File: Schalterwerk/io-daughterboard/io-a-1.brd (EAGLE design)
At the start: 80 x 30.5 mm, 34 parts, among them Q1 BSS123, Q2 BSS123, Q3 BSS123, Q4 BSS123, Q5 BSS123, Q6 BSS123, Q7 BSS123, Q8 BSS123, U1 74HC166, U2 74HC166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

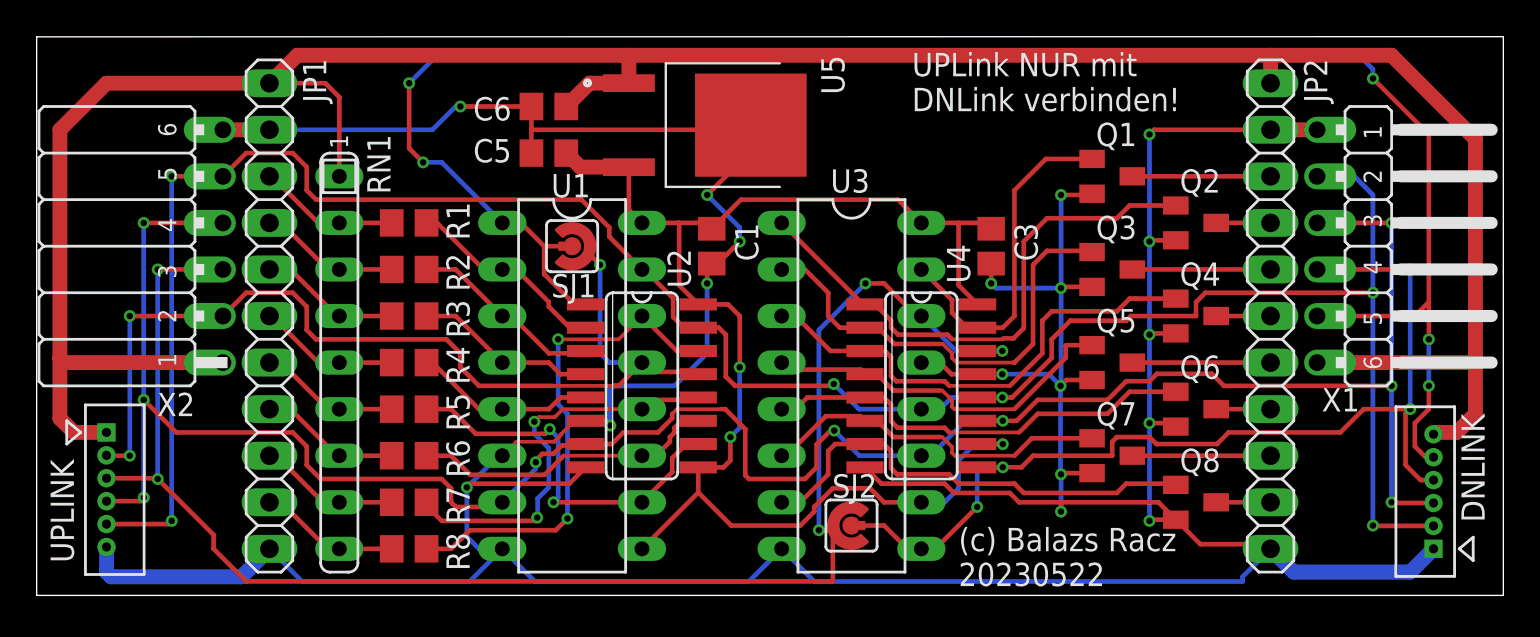
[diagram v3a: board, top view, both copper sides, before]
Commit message: Adds ground pour and connecting GND vias. Adds thermal-less poly under the regulator.
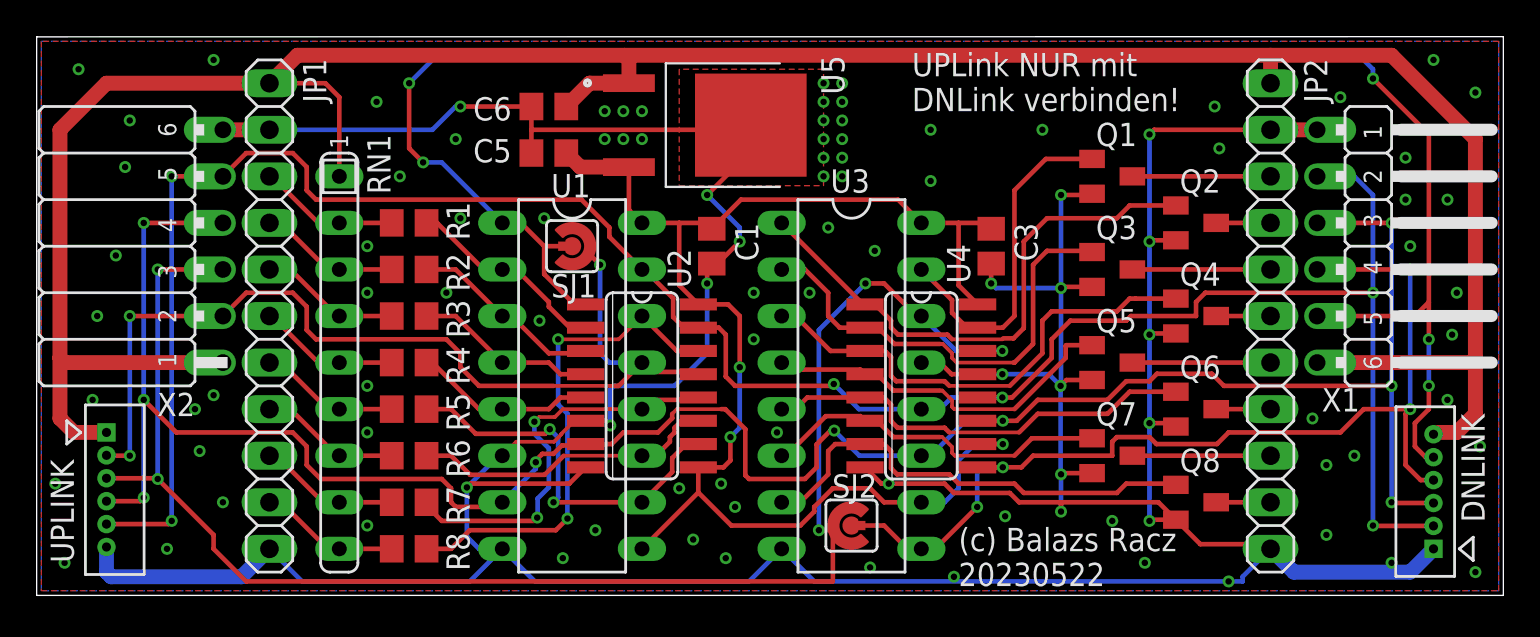
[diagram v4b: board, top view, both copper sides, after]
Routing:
- net GND: vias 18 -> 104
- added copper zone on layer 1, net GND
- added copper zone on layer 16, net GND
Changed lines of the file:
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@@
 <layer number="25" name="tNames" color="7" fill="1" visible="yes" active="yes"/>
 <layer number="26" name="bNames" color="7" fill="1" visible="yes" active="yes"/>
-<layer number="27" name="tValues" color="7" fill="1" visible="yes" active="yes"/>
+<layer number="27" name="tValues" color="7" fill="1" visible="no" active="yes"/>
 <layer number="28" name="bValues" color="7" fill="1" visible="no" active="yes"/>
 <layer number="29" name="tStop" color="7" fill="3" visible="no" active="yes"/>
@@
 <wire x1="6.35" y1="1.27" x2="6.35" y2="2.64" width="0.8128" layer="16"/>
 <wire x1="13.716" y1="1.016" x2="6.604" y2="1.016" width="0.8128" layer="16"/>
+<polygon width="0.1524" layer="1" isolate="0.254">
+<vertex x="2.794" y="30.226"/>
+<vertex x="2.794" y="0.254"/>
+<vertex x="82.296" y="0.254"/>
+<vertex x="82.296" y="30.226"/>
+</polygon>
+<polygon width="0.1524" layer="16" isolate="0.254">
+<vertex x="2.794" y="0.254"/>
+<vertex x="2.794" y="30.226"/>
+<vertex x="82.296" y="30.226"/>
+<vertex x="82.296" y="0.254"/>
+</polygon>
+<polygon width="0.1524" layer="1" thermals="no" rank="2">
+<vertex x="37.592" y="28.702"/>
+<vertex x="37.592" y="22.352"/>
+<vertex x="45.466" y="22.352"/>
+<vertex x="45.466" y="28.702"/>
+</polygon>
+<via x="45.466" y="26.924" extent="1-16" drill="0.35"/>
+<via x="45.466" y="25.908" extent="1-16" drill="0.35"/>
+<via x="45.466" y="24.892" extent="1-16" drill="0.35"/>
+<via x="45.466" y="23.876" extent="1-16" drill="0.35"/>
+<via x="45.466" y="22.86" extent="1-16" drill="0.35"/>
+<via x="46.482" y="26.924" extent="1-16" drill="0.35"/>
+<via x="46.482" y="25.908" extent="1-16" drill="0.35"/>
+<via x="46.482" y="24.892" extent="1-16" drill="0.35"/>
+<via x="46.482" y="23.876" extent="1-16" drill="0.35"/>
+<via x="46.482" y="22.86" extent="1-16" drill="0.35"/>
+<via x="33.528" y="26.416" extent="1-16" drill="0.35"/>
+<via x="34.544" y="26.416" extent="1-16" drill="0.35"/>
+<via x="35.56" y="26.416" extent="1-16" drill="0.35"/>
+<via x="33.528" y="24.892" extent="1-16" drill="0.35"/>
+<via x="34.544" y="24.892" extent="1-16" drill="0.35"/>
+<via x="35.56" y="24.892" extent="1-16" drill="0.35"/>
+<via x="51.308" y="25.4" extent="1-16" drill="0.35"/>
+<via x="57.404" y="25.4" extent="1-16" drill="0.35"/>
+<via x="66.802" y="26.67" extent="1-16" drill="0.35"/>
+<via x="67.056" y="24.384" extent="1-16" drill="0.35"/>
+<via x="21.082" y="26.924" extent="1-16" drill="0.35"/>
+<via x="22.352" y="22.86" extent="1-16" drill="0.35"/>
+<via x="25.4" y="24.892" extent="1-16" drill="0.35"/>
+<via x="7.62" y="25.908" extent="1-16" drill="0.35"/>
+<via x="7.366" y="23.368" extent="1-16" drill="0.35"/>
+<via x="6.858" y="18.542" extent="1-16" drill="0.35"/>
+<via x="4.826" y="28.702" extent="1-16" drill="0.35"/>
+<via x="12.192" y="29.21" extent="1-16" drill="0.35"/>
+<via x="5.842" y="15.24" extent="1-16" drill="0.35"/>
+<via x="12.192" y="10.922" extent="1-16" drill="0.35"/>
+<via x="11.176" y="10.16" extent="1-16" drill="0.35"/>
+<via x="11.43" y="7.874" extent="1-16" drill="0.35"/>
+<via x="12.7" y="5.08" extent="1-16" drill="0.35"/>
+<via x="5.588" y="10.668" extent="1-16" drill="0.35"/>
+<via x="3.556" y="6.096" extent="1-16" drill="0.35"/>
+<via x="4.064" y="1.778" extent="1-16" drill="0.35"/>
+<via x="9.652" y="2.54" extent="1-16" drill="0.35"/>
+<via x="31.242" y="2.032" extent="1-16" drill="0.35"/>
+<via x="33.02" y="3.556" extent="1-16" drill="0.35"/>
+<via x="20.574" y="3.81" extent="1-16" drill="0.35"/>
+<via x="20.574" y="8.89" extent="1-16" drill="0.35"/>
+<via x="20.574" y="11.43" extent="1-16" drill="0.35"/>
+<via x="20.574" y="16.51" extent="1-16" drill="0.35"/>
+<via x="24.892" y="16.51" extent="1-16" drill="0.35"/>
+<via x="20.574" y="19.05" extent="1-16" drill="0.35"/>
+<via x="25.654" y="20.574" extent="1-16" drill="0.35"/>
+<via x="30.226" y="20.574" extent="1-16" drill="0.35"/>
+<via x="29.972" y="14.986" extent="1-16" drill="0.35"/>
+<via x="39.878" y="6.096" extent="1-16" drill="0.35"/>
+<via x="40.64" y="4.826" extent="1-16" drill="0.35"/>
+<via x="38.354" y="3.048" extent="1-16" drill="0.35"/>
+<via x="40.132" y="2.032" extent="1-16" drill="0.35"/>
+<via x="48.006" y="1.524" extent="1-16" drill="0.35"/>
+<via x="52.578" y="1.016" extent="1-16" drill="0.35"/>
+<via x="55.372" y="4.318" extent="1-16" drill="0.35"/>
+<via x="62.992" y="1.778" extent="1-16" drill="0.35"/>
+<via x="67.564" y="0.762" extent="1-16" drill="0.35"/>
+<via x="72.898" y="7.112" extent="1-16" drill="0.35"/>
+<via x="74.422" y="7.62" extent="1-16" drill="0.35"/>
+<via x="72.898" y="3.302" extent="1-16" drill="0.35"/>
+<via x="76.454" y="1.778" extent="1-16" drill="0.35"/>
+<via x="81.026" y="1.27" extent="1-16" drill="0.35"/>
+<via x="81.28" y="8.128" extent="1-16" drill="0.35"/>
+<via x="79.502" y="10.668" extent="1-16" drill="0.35"/>
+<via x="79.756" y="14.224" extent="1-16" drill="0.35"/>
+<via x="80.01" y="16.51" extent="1-16" drill="0.35"/>
+<via x="79.502" y="21.59" extent="1-16" drill="0.35"/>
+<via x="77.216" y="23.876" extent="1-16" drill="0.35"/>
+<via x="73.66" y="27.178" extent="1-16" drill="0.35"/>
+<via x="77.216" y="21.59" extent="1-16" drill="0.35"/>
+<via x="77.47" y="19.05" extent="1-16" drill="0.35"/>
+<via x="78.74" y="29.21" extent="1-16" drill="0.35"/>
+<via x="81.026" y="27.432" extent="1-16" drill="0.35"/>
+<via x="72.136" y="9.652" extent="1-16" drill="0.35"/>
+<via x="61.214" y="4.064" extent="1-16" drill="0.35"/>
+<via x="42.926" y="8.89" extent="1-16" drill="0.35"/>
+<via x="41.656" y="13.97" extent="1-16" drill="0.35"/>
+<via x="41.656" y="16.51" extent="1-16" drill="0.35"/>
+<via x="44.704" y="16.51" extent="1-16" drill="0.35"/>
+<via x="45.72" y="20.066" extent="1-16" drill="0.35"/>
+<via x="48.26" y="18.796" extent="1-16" drill="0.35"/>
+<via x="51.308" y="22.606" extent="1-16" drill="0.35"/>
+<via x="45.466" y="27.94" extent="1-16" drill="0.35"/>
+<via x="46.482" y="27.94" extent="1-16" drill="0.35"/>
+<via x="37.592" y="5.842" extent="1-16" drill="0.35"/>
+<via x="49.022" y="6.096" extent="1-16" drill="0.35"/>
 </signal>
 <signal name="MISO-DN">
@@
 <wire x1="7.62" y1="7.62" x2="6.37" y2="7.62" width="0.254" layer="1"/>
 <wire x1="6.37" y1="7.62" x2="6.35" y2="7.64" width="0.254" layer="1"/>
-<wire x1="7.62" y1="15.24" x2="12.7" y2="15.24" width="0" layer="19"/>
 </signal>
 <signal name="LATCH">
@@
 <wire x1="43.18" y1="15.24" x2="43.942" y2="15.24" width="0.254" layer="1"/>
 <wire x1="45.847" y1="13.335" x2="47.7266" y2="13.335" width="0.254" layer="1"/>
+<wire x1="64.686" y1="16.189996875" x2="64.686" y2="16.19" width="0" layer="19" extent="1-1"/>
 </signal>
 <signal name="N$27">

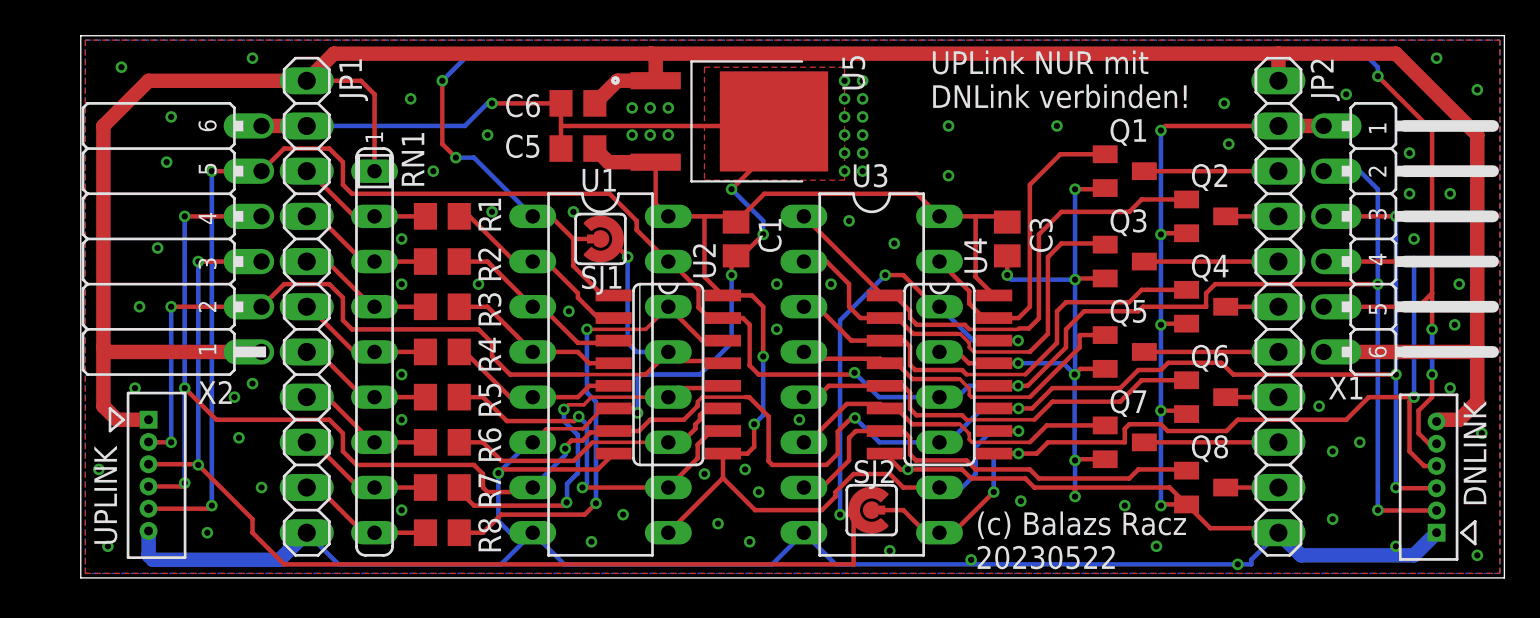
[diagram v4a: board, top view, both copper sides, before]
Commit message: Updates layout of the io daughterboard. Updates silkscreen documentation.
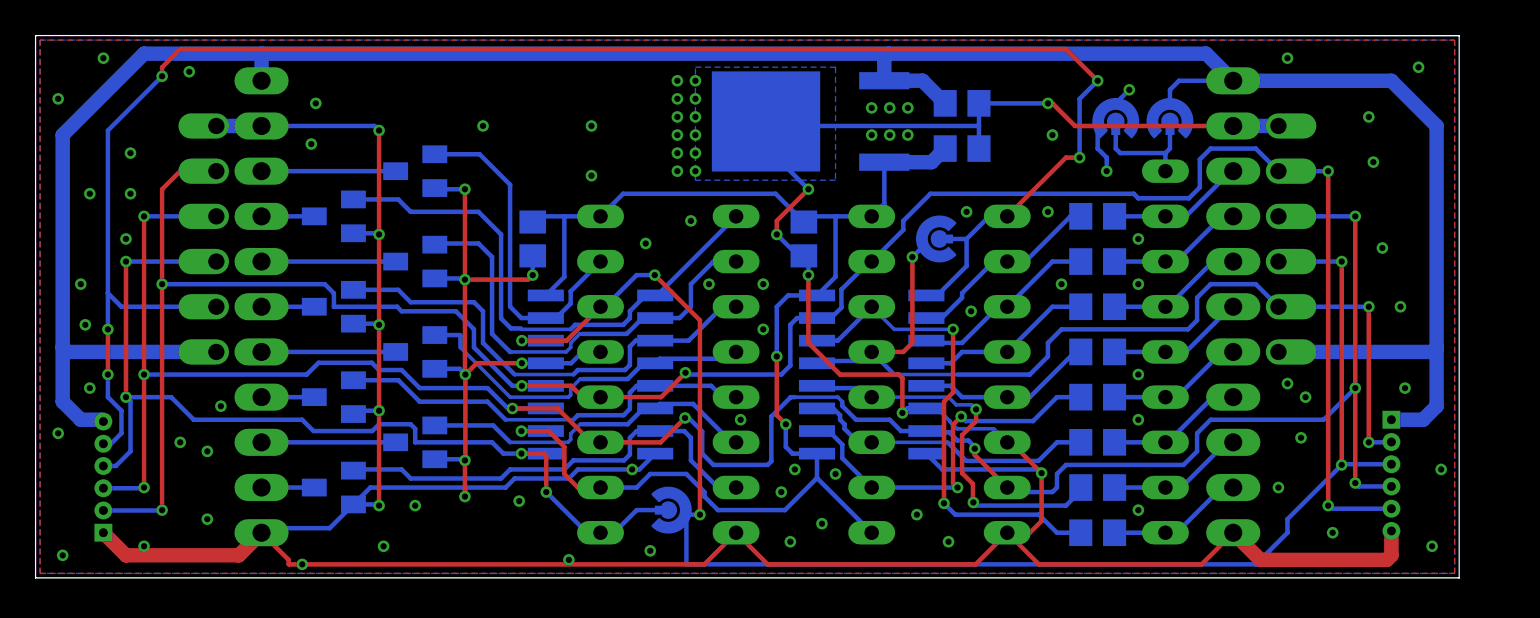
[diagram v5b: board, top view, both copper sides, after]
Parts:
- added SJ3, SJ4: (no value), trainlib:SJ_RND2
- moved X4 74.9 mm to (3.81, 2.54), flipped to the bottom
- moved X3 69.9 mm to (76.2, 8.89), flipped to the bottom
- moved X1 62.2 mm to (10.2, 16.5), flipped to the bottom
- moved JP2 57.1 mm to (12.7, 15.2), flipped to the bottom
- moved X2 57.1 mm to (69.8, 21.6), flipped to the bottom
- moved JP1 52.1 mm to (67.3, 15.2), flipped to the bottom
- moved Q2 49.0 mm to (16.8, 20.3), flipped to the bottom
- moved Q4 49.0 mm to (16.8, 15.2), flipped to the bottom
- moved Q6 49.0 mm to (16.8, 10.2), flipped to the bottom
- moved Q8 49.0 mm to (16.8, 5.08), flipped to the bottom
- moved RN1 44.5 mm to (63.5, 12.7), flipped to the bottom
- moved Q1 39.9 mm to (21.3, 22.9), flipped to the bottom
- moved Q3 39.9 mm to (21.3, 17.8), flipped to the bottom
- moved Q5 39.9 mm to (21.3, 12.7), flipped to the bottom
- moved Q7 39.9 mm to (21.3, 7.62), flipped to the bottom
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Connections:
- new net N$1: RN1.1, SJ3.P$1, SJ4.P$1
- net +12V: now also SJ3.P$2; no longer RN1.1
- net GND: now also SJ4.P$2
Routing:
- net N$1: track 0.00 -> 6.81 mm
- net GND: track 254.4 -> 260.2 mm
- net +12V: track 150.4 -> 146.5 mm
- net SCK: track 126.3 -> 126.8 mm
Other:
- board text added: "(c) Balazs Racz 20230526"
- board text added: "I/O"
- board text removed: "(c) Balazs Racz 20230522"
